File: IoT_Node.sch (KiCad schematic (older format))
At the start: 73 parts

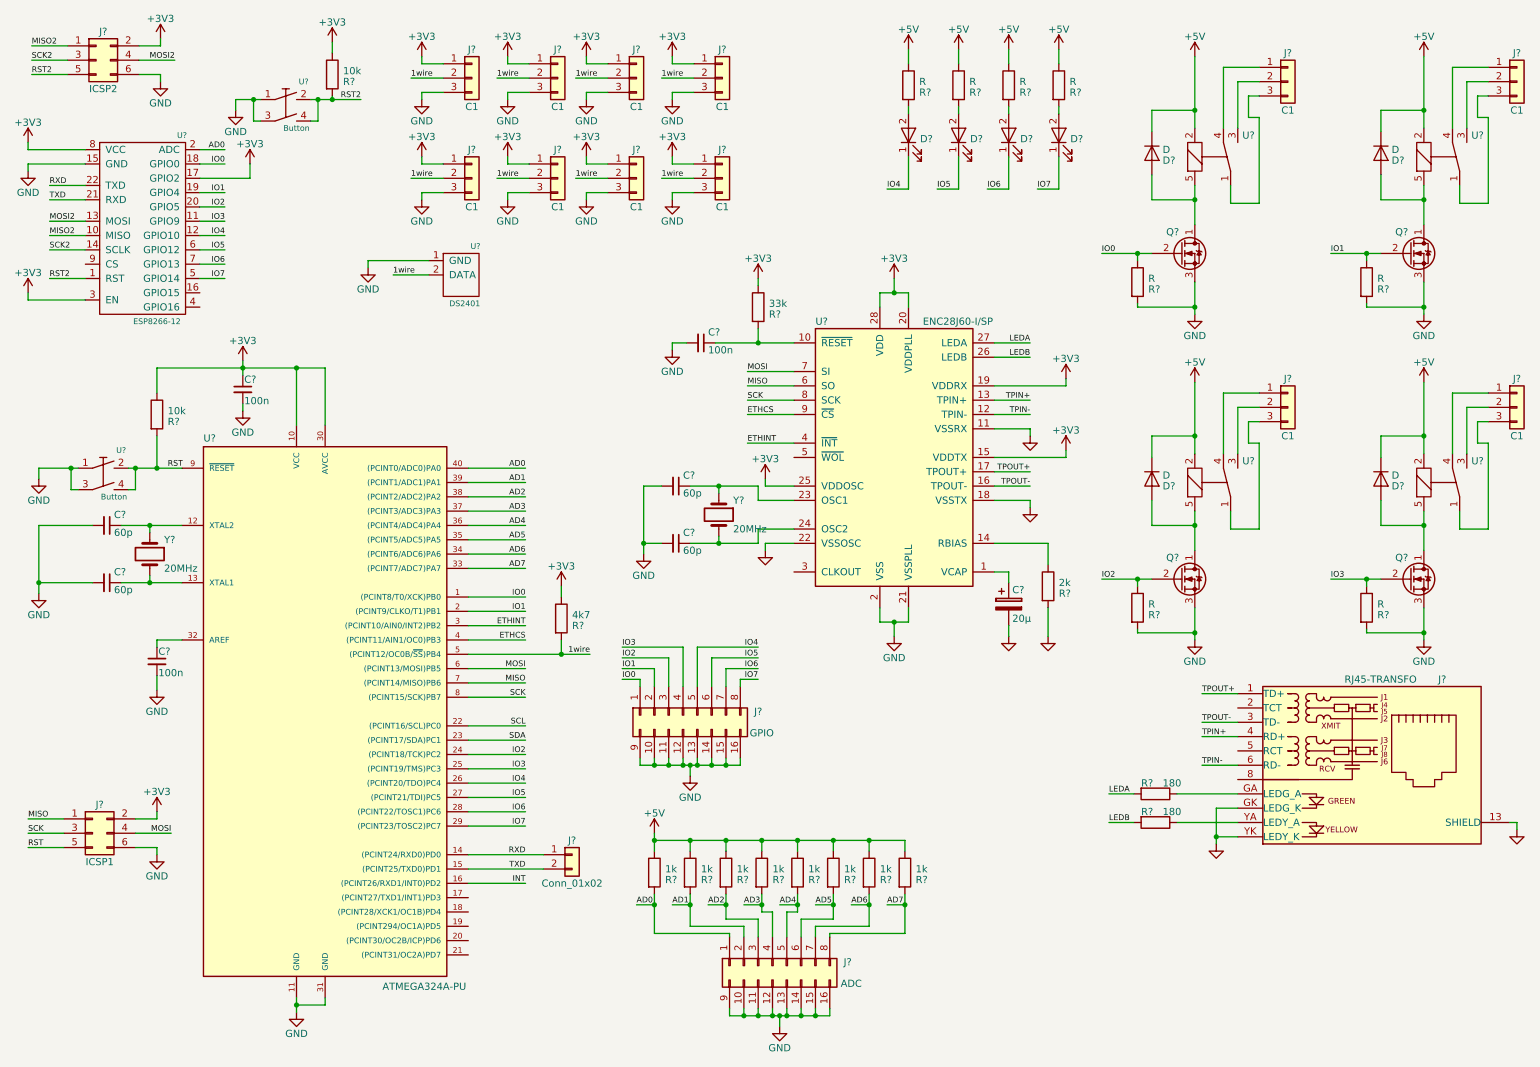
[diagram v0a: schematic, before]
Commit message: Footprints assigned
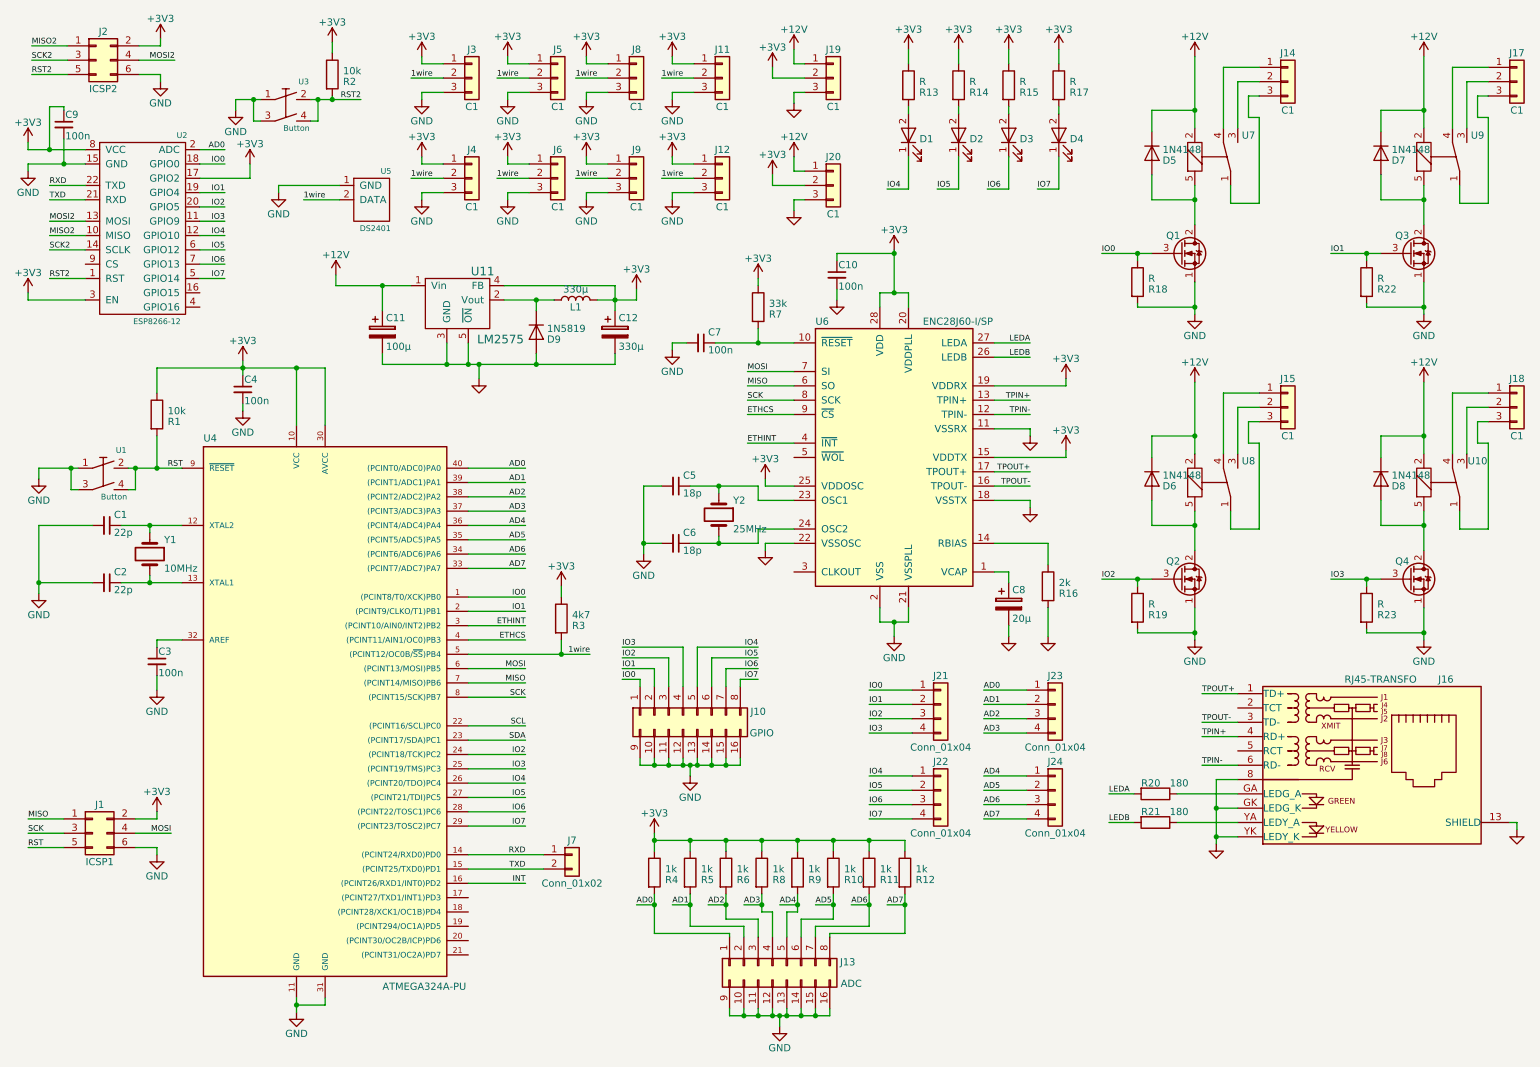
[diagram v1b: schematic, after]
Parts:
- removed Q? (x4): Q_NMOS_DGS, symbol Q_NMOS_DGS
- removed U? (x3): Relay, symbol Relay
- added C10, C9: 100n, Capacitors_ThroughHole:C_Rect_L4.0mm_W2.5mm_P2.50mm, symbol C_Small
- added C11: 100µ, Capacitors_ThroughHole:CP_Radial_Tantal_D7.0mm_P5.00mm, symbol CP
- added C12: 330µ, Capacitors_ThroughHole:CP_Radial_D10.0mm_P5.00mm, symbol CP
- added D9: 1N5819, Diodes_ThroughHole:D_DO-41_SOD81_P7.62mm_Horizontal, symbol D
- added J19, J20: C1, Terminal_Blocks:TerminalBlock_bornier-3_P5.08mm, symbol Conn_01x03
- added J21, J22, J23, J24: Conn_01x04, Terminal_Blocks:TerminalBlock_bornier-4_P5.08mm, symbol Conn_01x04
- added L1: 330µ, Capacitors_ThroughHole:CP_Radial_D13.0mm_P7.50mm, symbol L
- added Q1, Q2, Q3, Q4: Q_NMOS_SDG, TO_SOT_Packages_THT:TO-92_Inline_Wide, symbol Q_NMOS_SDG
- added U10, U8, U9: Relay, Relays_ThroughHole:Relay_SPDT_OMRON-G5LE-1, symbol Relay
- added U11: LM2575, TO_SOT_Packages_THT:TO-220-5_Vertical, symbol LM2575
- C1, C2: renamed from C?; value 60p -> 22p; footprint (none) -> Capacitors_ThroughHole:C_Rect_L4.0mm_W2.5mm_P2.50mm
- C3, C4, C7: renamed from C?; footprint (none) -> Capacitors_ThroughHole:C_Rect_L4.0mm_W2.5mm_P2.50mm
- C5, C6: renamed from C?; value 60p -> 18p; footprint (none) -> Capacitors_ThroughHole:C_Rect_L4.0mm_W2.5mm_P2.50mm
- C8: renamed from C?; footprint (none) -> Capacitors_ThroughHole:CP_Radial_D5.0mm_P2.00mm
- D1, D2, D3, D4: renamed from D?; footprint (none) -> LEDs:LED_D5.0mm
- D5, D6, D7, D8: renamed from D?; value D -> 1N4148; footprint (none) -> Diodes_ThroughHole:D_DO-35_SOD27_P7.62mm_Horizontal
- J1, J2: renamed from J?; footprint (none) -> Socket_Strips:Socket_Strip_Straight_2x03_Pitch2.54mm
- J10, J13: renamed from J?; footprint (none) -> Socket_Strips:Socket_Strip_Straight_2x08_Pitch2.54mm
- J11, J12, J14, J15, J17, J18, J3, J4, J5, J6, J8, J9: renamed from J?; footprint (none) -> Terminal_Blocks:TerminalBlock_bornier-3_P5.08mm
- J16: renamed from J?; footprint (none) -> Bauteile:RJ45-WIZnet
- J7: renamed from J?; footprint (none) -> Socket_Strips:Socket_Strip_Angled_1x02_Pitch2.54mm
- R1, R10, R11, R12, R13, R14, R15, R16, R17, R18, R19, R2, R20, R21, R22, R23, R3, R4, R5, R6, R7, R8, R9: renamed from R?; footprint (none) -> Resistors_ThroughHole:R_Axial_DIN0207_L6.3mm_D2.5mm_P10.16mm_Horizontal
- U1, U3: renamed from U?; footprint (none) -> Buttons_Switches_ThroughHole:SW_TH_Tactile_Omron_B3F-10xx
- U2: renamed from U?; footprint (none) -> ESP8266:ESP-12E_SMD
- U4: renamed from U?; footprint DIL40 -> Housings_DIP:DIP-40_W15.24mm_LongPads
- U5: renamed from U?; footprint (none) -> TO_SOT_Packages_THT:TO-92_Inline_Narrow_Oval
- U6: renamed from U?; footprint DIP-28 -> Housings_DIP:DIP-28_W7.62mm_LongPads
- U7: renamed from U?; footprint (none) -> Relays_ThroughHole:Relay_SPDT_OMRON-G5LE-1
- Y1: renamed from Y?; value 20MHz -> 10MHz; footprint (none) -> Crystals:Crystal_HC49-4H_Vertical
- Y2: renamed from Y?; value 20MHz -> 25MHz; footprint (none) -> Crystals:Crystal_HC49-4H_Vertical
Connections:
- net +3V3: now also R10.1, R11.1, R12.1, R13.1, R14.1, R15.1, R17.1, R4.1, R5.1, R6.1, R8.1, R9.1, C10.1, C12.1, C9.1, J19.2 (Pin_2), J20.2 (Pin_2), L1.2, U11.4 (FB)
- net AD0: now also J23.1 (Pin_1)
- net AD1: now also J23.2 (Pin_2)
- net AD2: now also J23.3 (Pin_3)
- net AD3: now also J23.4 (Pin_4)
- net AD4: now also J24.1 (Pin_1)
- net AD5: now also J24.2 (Pin_2)
- net AD6: now also J24.3 (Pin_3)
- net AD7: now also J24.4 (Pin_4)
- net GND: now also J16.8, C10.2, C11.2, C12.2, C9.2, D9.2 (A), J19.3 (Pin_3), J20.3 (Pin_3), Q1.1 (S), Q2.1 (S), Q3.1 (S), Q4.1 (S), U11.3 (GND), U11.5 (~ON)
- net IO0: now also J21.1 (Pin_1), Q1.3 (G)
- net IO1: now also J21.2 (Pin_2), Q3.3 (G)
- net IO2: now also J21.3 (Pin_3), Q2.3 (G)
- net IO3: now also J21.4 (Pin_4), Q4.3 (G)
- net IO4: now also J22.1 (Pin_1)
- net IO5: now also J22.2 (Pin_2)
- net IO6: now also J22.3 (Pin_3)
- net IO7: now also J22.4 (Pin_4)
- net at J17.3 (Pin_3): now also U9.1
- net at J17.2 (Pin_2): now also U9.3
- net at J17.1 (Pin_1): now also U9.4
- net at D7.2 (A): now also Q3.2 (D), U9.5
- net at D5.2 (A), U7.5: now also Q1.2 (D)
- net at J18.3 (Pin_3): now also U10.1
- net at J18.2 (Pin_2): now also U10.3
- net at J18.1 (Pin_1): now also U10.4
- net at D8.2 (A): now also Q4.2 (D), U10.5
- net at J15.3 (Pin_3): now also U8.1
- net at J15.2 (Pin_2): now also U8.3
- net at J15.1 (Pin_1): now also U8.4
- net at D6.2 (A): now also Q2.2 (D), U8.5
- removed net +5V: D5.1 (K), D6.1 (K), D7.1 (K), D8.1 (K), R10.1, R11.1, R12.1, R13.1, R14.1, R15.1, R17.1, R4.1, R5.1, R6.1, R8.1, R9.1, U7.2
- new net: D9.1 (K), L1.1, U11.2 (Vout)
- new net +12V: C11.1, D5.1 (K), D6.1 (K), D7.1 (K), D8.1 (K), J19.1 (Pin_1), J20.1 (Pin_1), U10.2, U11.1 (Vin), U7.2, U8.2, U9.2
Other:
- moved on the sheet: U5
